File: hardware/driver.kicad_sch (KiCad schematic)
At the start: 21 parts, among them U4 EPC2152, U5 EPC2152, U6 INA181A2IDBVT, U7 INA181A2IDBVT, U8 EPC2152, U9 INA181A2IDBVT

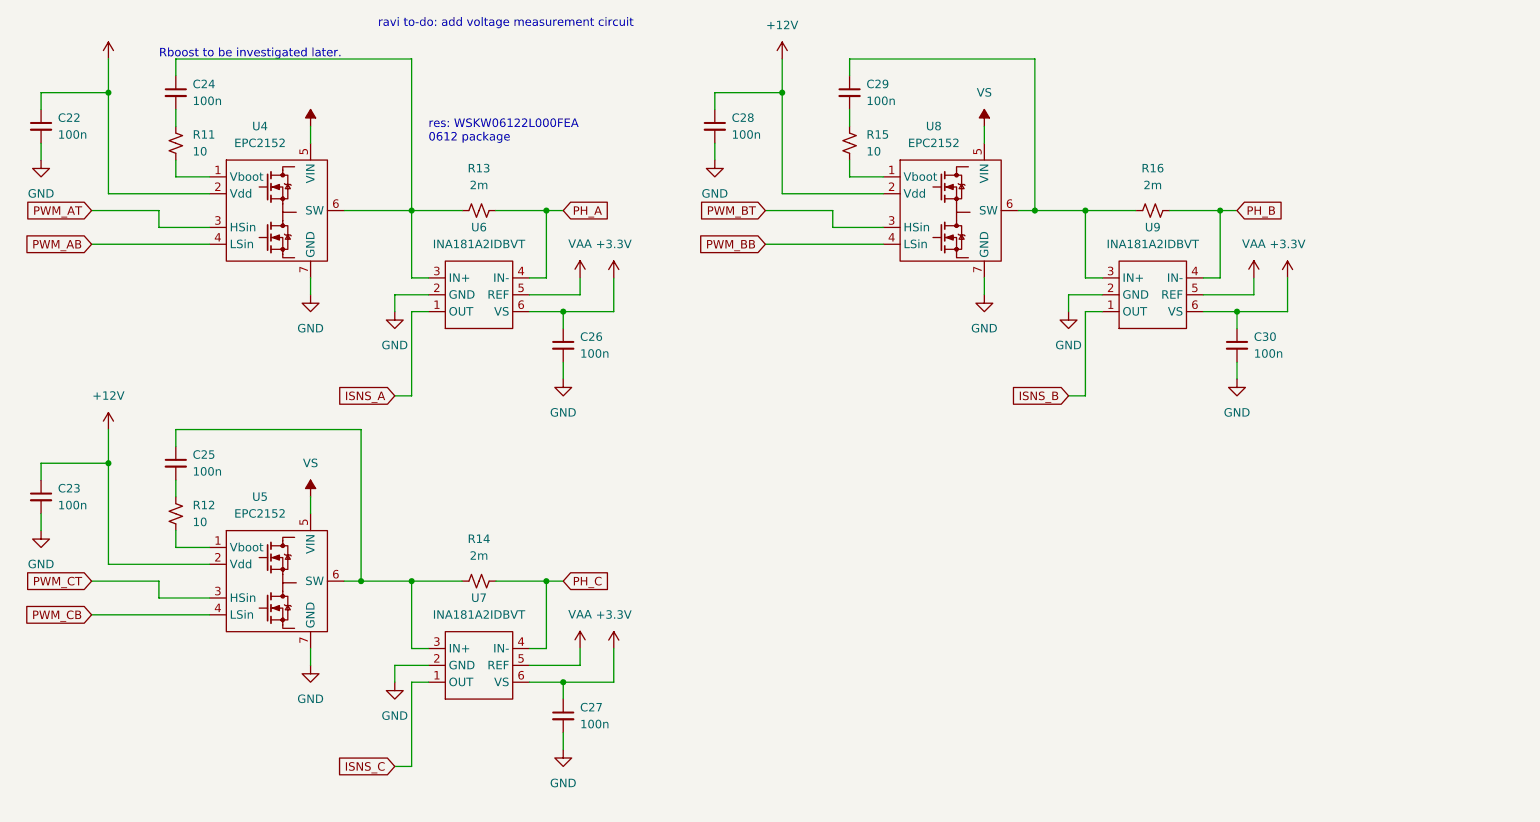
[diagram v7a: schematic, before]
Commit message: signal leds, bulk capacitance
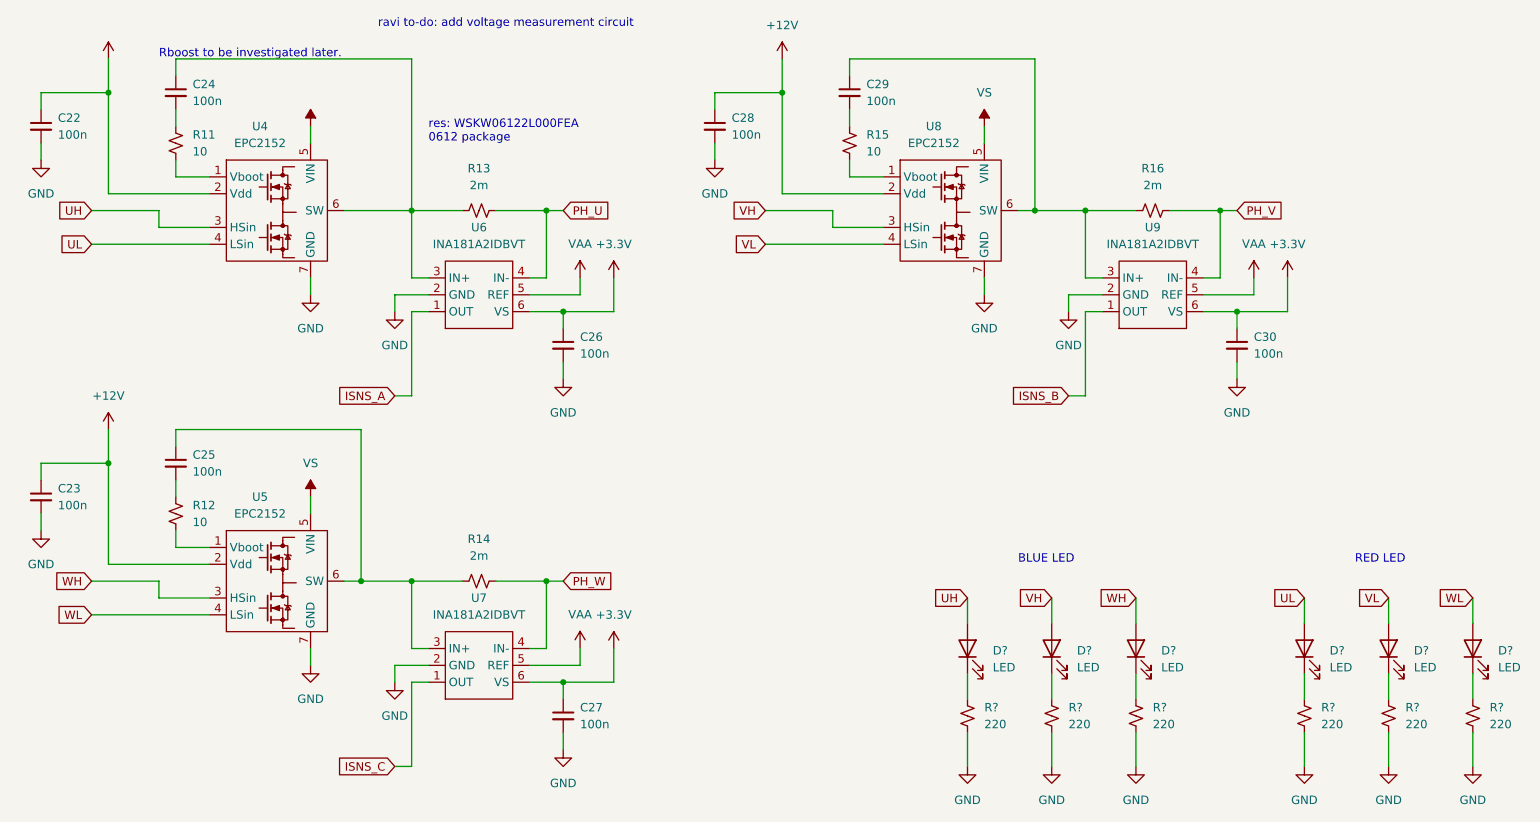
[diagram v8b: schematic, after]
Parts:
- added D? (x6): LED, symbol Device:LED
- added R? (x6): 220, Resistor_SMD:R_0805_2012Metric, symbol Device:R_Small_US
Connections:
- net GND: now also R?.2, R?.2, R?.2, R?.2, R?.2, R?.2
- net PH_A renamed PH_U
- net PH_B renamed PH_V
- net PH_C renamed PH_W
- net PWM_AB renamed UL
- net UL: now also D?.2 (A)
- net PWM_AT renamed UH
- net UH: now also D?.2 (A)
- net PWM_BB renamed VL
- net VL: now also D?.2 (A)
- net PWM_BT renamed VH
- net VH: now also D?.2 (A)
- net PWM_CB renamed WL
- net WL: now also D?.2 (A)
- net PWM_CT renamed WH
- net WH: now also D?.2 (A)
- new net: D?.1 (K), R?.1 (x6)
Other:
- note added: "BLUE LED"
- note added: "RED LED"
